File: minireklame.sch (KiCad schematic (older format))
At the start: 33 parts, among them IC1 ATXMEGA64A4U-A, P1 CONN_01X02, P10 CONN_01X04, P11 CONN_01X04, P12 CONN_01X04, P13 CONN_01X04, P14 CONN_01X04, P15 CONN_01X04, P16 CONN_01X04, P17 CONN_01X04, P2 CONN_01X04, P3 CONN_01X02, P3 CONN_01X04, P4 CONN_01X04, P5 CONN_01X04, P6 CONN_01X04, P7 CONN_01X04, P8 CONN_01X04, P9 CONN_01X04, U1 TLV1117-33CDCYR, U2 SP3483-EN-L, U3 TLC5955

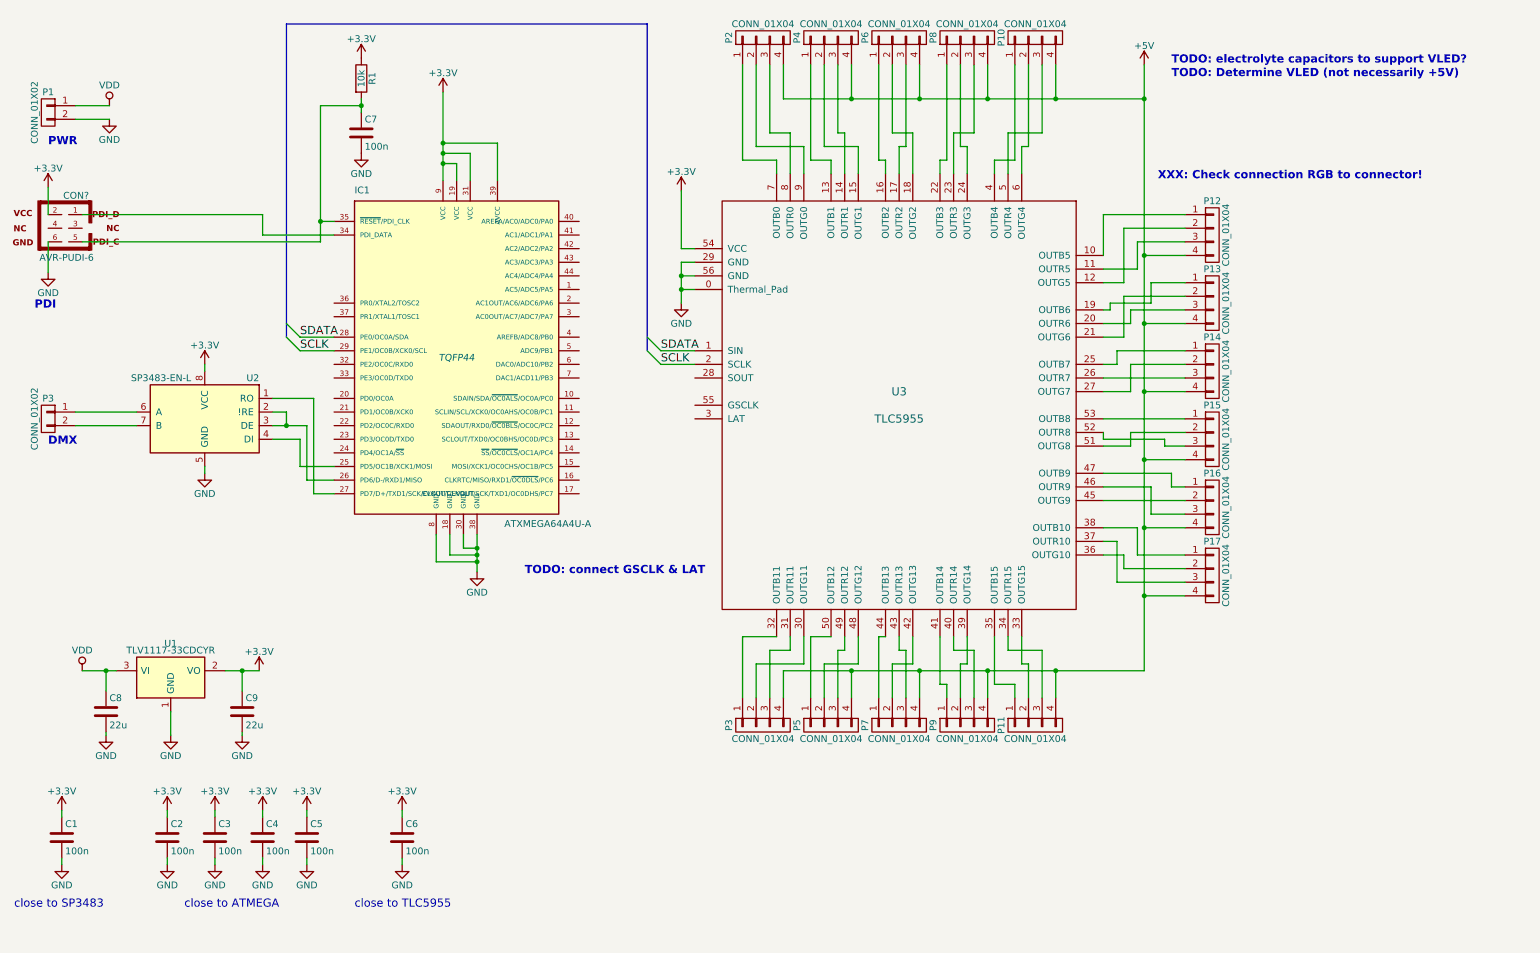
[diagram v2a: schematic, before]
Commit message: pulldown for & !RE DE line
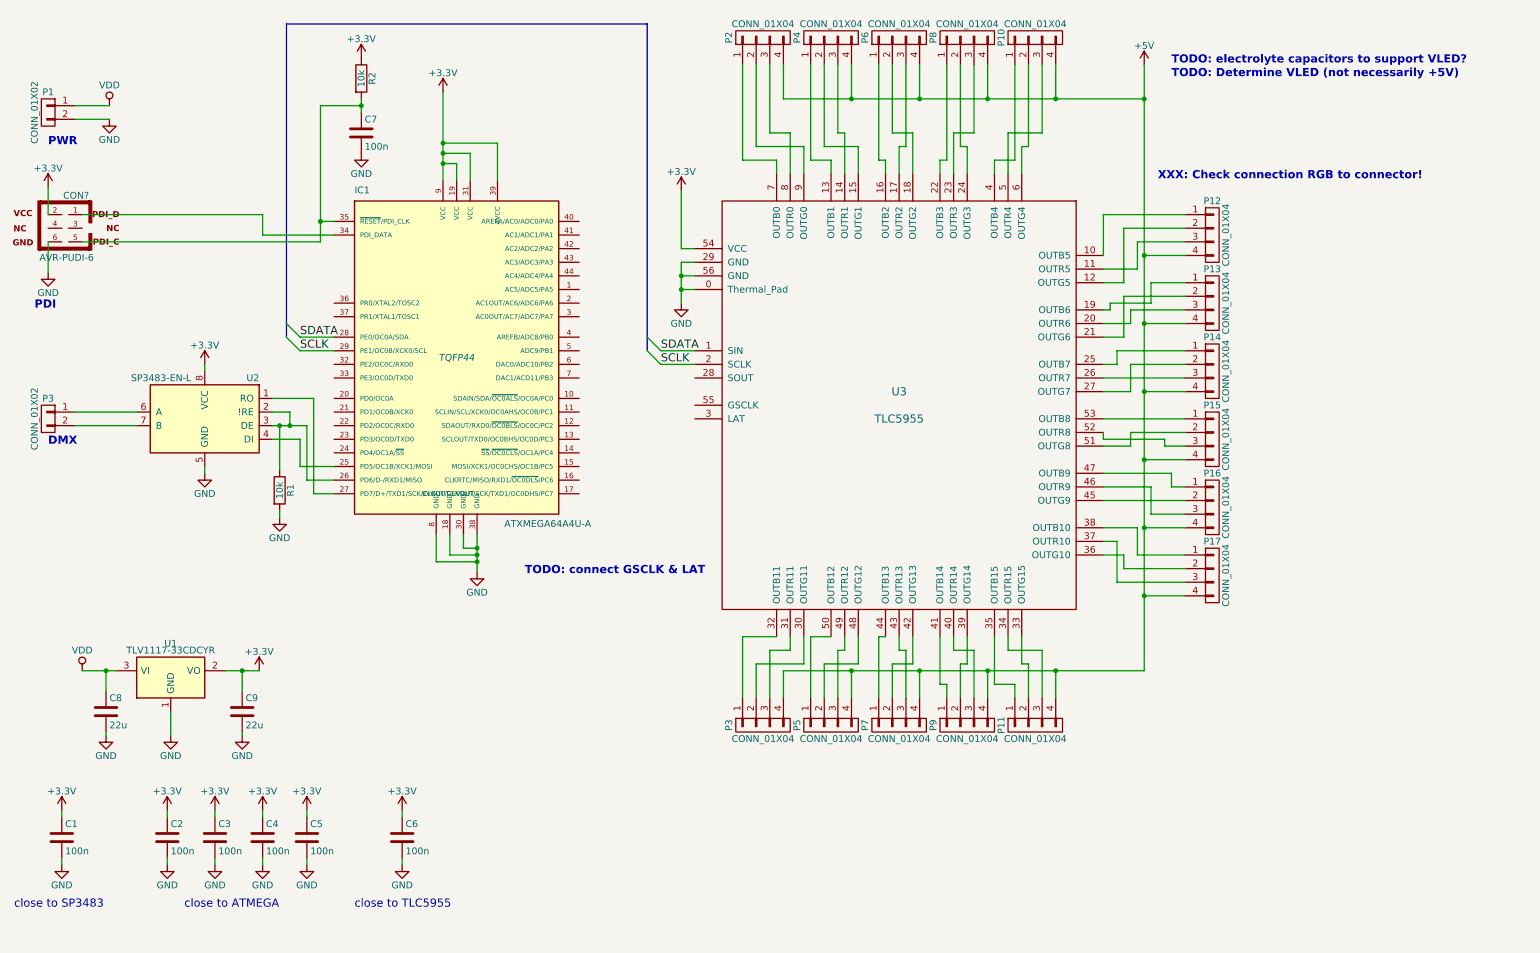
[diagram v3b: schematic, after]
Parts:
- added R1: 10k, symbol R
- renumbered R1 to R2
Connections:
- net GND: now also R1.2
- net at IC1.26 (PD6/D-/RXD1/MISO), U2.2 (!RE), U2.3 (DE): now also R1.1
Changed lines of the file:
@@
 	3700 4600 3700 4800
 Wire Wire Line
-	4000 4600 4000 4875
+	4000 4600 4000 4700
+Wire Wire Line
+	4000 4700 4000 4750
+Wire Wire Line
+	4000 4750 4000 4800
+Wire Wire Line
+	4000 4800 4000 4875
 Wire Wire Line
 	3900 4600 3900 4700
@@
 	5500 2800 5600 2800
 Wire Wire Line
-	5500 2600 5500 2900
+	5500 2600 5500 2700
+Wire Wire Line
+	5500 2700 5500 2800
+Wire Wire Line
+	5500 2800 5500 2900
 Wire Wire Line
 	5600 2700 5500 2700
@@
 Connection ~ 5500 2700
 Wire Wire Line
-	3750 1350 3750 2000
+	3750 1350 3750 1725
+Wire Wire Line
+	3750 1725 3750 1800
+Wire Wire Line
+	3750 1800 3750 1875
+Wire Wire Line
+	3750 1875 3750 2000
 Wire Wire Line
 	5500 2500 5600 2500
@@
 	5600 3350 5350 3350
 Wire Bus Line
-	5250 850  5250 3250
+	5250 850  5250 3150
+Wire Bus Line
+	5250 3150 5250 3250
 Wire Bus Line
 	5250 850  2600 850
 Wire Bus Line
-	2600 850  2600 3150
+	2600 850  2600 3050
+Wire Bus Line
+	2600 3050 2600 3150
 Wire Wire Line
 	2700 3150 2950 3150
@@
 	2700 4100 2950 4100
 Wire Wire Line
-	2500 3800 2750 3800
+	2500 3800 2550 3800
+Wire Wire Line
+	2550 3800 2625 3800
+Wire Wire Line
+	2625 3800 2750 3800
 Wire Wire Line
 	2750 3800 2750 4200
@@
 	2750 4200 2950 4200
 Wire Wire Line
-	2500 3700 2600 3700
-Wire Wire Line
-	2600 3700 2600 3800
-Connection ~ 2600 3800
+	2500 3700 2625 3700
+Wire Wire Line
+	2625 3700 2625 3800
+Connection ~ 2625 3800
 Wire Wire Line
 	2500 3600 2800 3600
@@
 	6250 1150 6250 1400
 Wire Wire Line
-	6250 1400 8900 1400
-Wire Wire Line
-	8900 5600 8900 1150
+	6250 1400 6750 1400
+Wire Wire Line
+	6750 1400 7250 1400
+Wire Wire Line
+	7250 1400 7750 1400
+Wire Wire Line
+	7750 1400 8250 1400
+Wire Wire Line
+	8250 1400 8900 1400
+Wire Wire Line
+	8900 5600 8900 5050
+Wire Wire Line
+	8900 5050 8900 4550
+Wire Wire Line
+	8900 4550 8900 4050
+Wire Wire Line
+	8900 4050 8900 3550
+Wire Wire Line
+	8900 3550 8900 3050
+Wire Wire Line
+	8900 3050 8900 2550
+Wire Wire Line
+	8900 2550 8900 1400
+Wire Wire Line
+	8900 1400 8900 1150
 Wire Wire Line
 	6750 1150 6750 1400
@@
 	6250 5800 6250 5600
 Wire Wire Line
-	6250 5600 8900 5600
+	6250 5600 6750 5600
+Wire Wire Line
+	6750 5600 7250 5600
+Wire Wire Line
+	7250 5600 7750 5600
+Wire Wire Line
+	7750 5600 8250 5600
+Wire Wire Line
+	8250 5600 8900 5600
 Connection ~ 8900 5050
 Wire Wire Line
@@
 $EndComp
 Wire Wire Line
-	1100 5600 1350 5600
+	1100 5600 1275 5600
+Wire Wire Line
+	1275 5600 1350 5600
 $Comp
 L GND #PWR012
@@
 TODO: Determine VLED (not necessarily +5V)
 $Comp
-L R R1
+L R R2
 U 1 1 58DDA6F7
 P 3150 1250
-F 0 "R1" V 3230 1250 50  0000 C CNN
+F 0 "R2" V 3230 1250 50  0000 C CNN
 F 1 "10k" V 3150 1250 50  0000 C CNN
 F 2 "" V 3080 1250 50  0001 C CNN
@@
 	2850 1450 3150 1450
 Wire Wire Line
-	3150 1400 3150 1500
+	3150 1400 3150 1450
+Wire Wire Line
+	3150 1450 3150 1500
 Connection ~ 3150 1450
 $Comp
@@
 	1050 1550 1300 1550
 Wire Wire Line
-	2850 1450 2850 2450
+	2850 1450 2850 2300
+Wire Wire Line
+	2850 2300 2850 2450
 Text Notes 850  1750 0    60   ~ 12
 PWR
@@
 	1750 5900 1750 6075
 Wire Wire Line
-	2150 5600 2400 5600
+	2150 5600 2275 5600
+Wire Wire Line
+	2275 5600 2400 5600
 Wire Wire Line
 	2275 5750 2275 5600
@@
 Wire Wire Line
 	5600 2600 5500 2600
+$Comp
+L R R1
+U 1 1 591A7EA8
+P 2550 4275
+F 0 "R1" V 2630 4275 50  0000 C CNN
+F 1 "10k" V 2550 4275 50  0000 C CNN
+F 2 "" V 2480 4275 50  0001 C CNN
+F 3 "" H 2550 4275 50  0001 C CNN
+	1    2550 4275
+	1    0    0    -1
+$EndComp
+$Comp
+L GND #PWR?
+U 1 1 591A821A
+P 2550 4475
+F 0 "#PWR?" H 2550 4225 50  0001 C CNN
+F 1 "GND" H 2550 4325 50  0000 C CNN
+F 2 "" H 2550 4475 50  0000 C CNN
+F 3 "" H 2550 4475 50  0000 C CNN
+	1    2550 4475
+	1    0    0    -1
+$EndComp
+Wire Wire Line
+	2550 4475 2550 4425
+Wire Wire Line
+	2550 4125 2550 3800
+Connection ~ 2550 3800
 $EndSCHEMATC

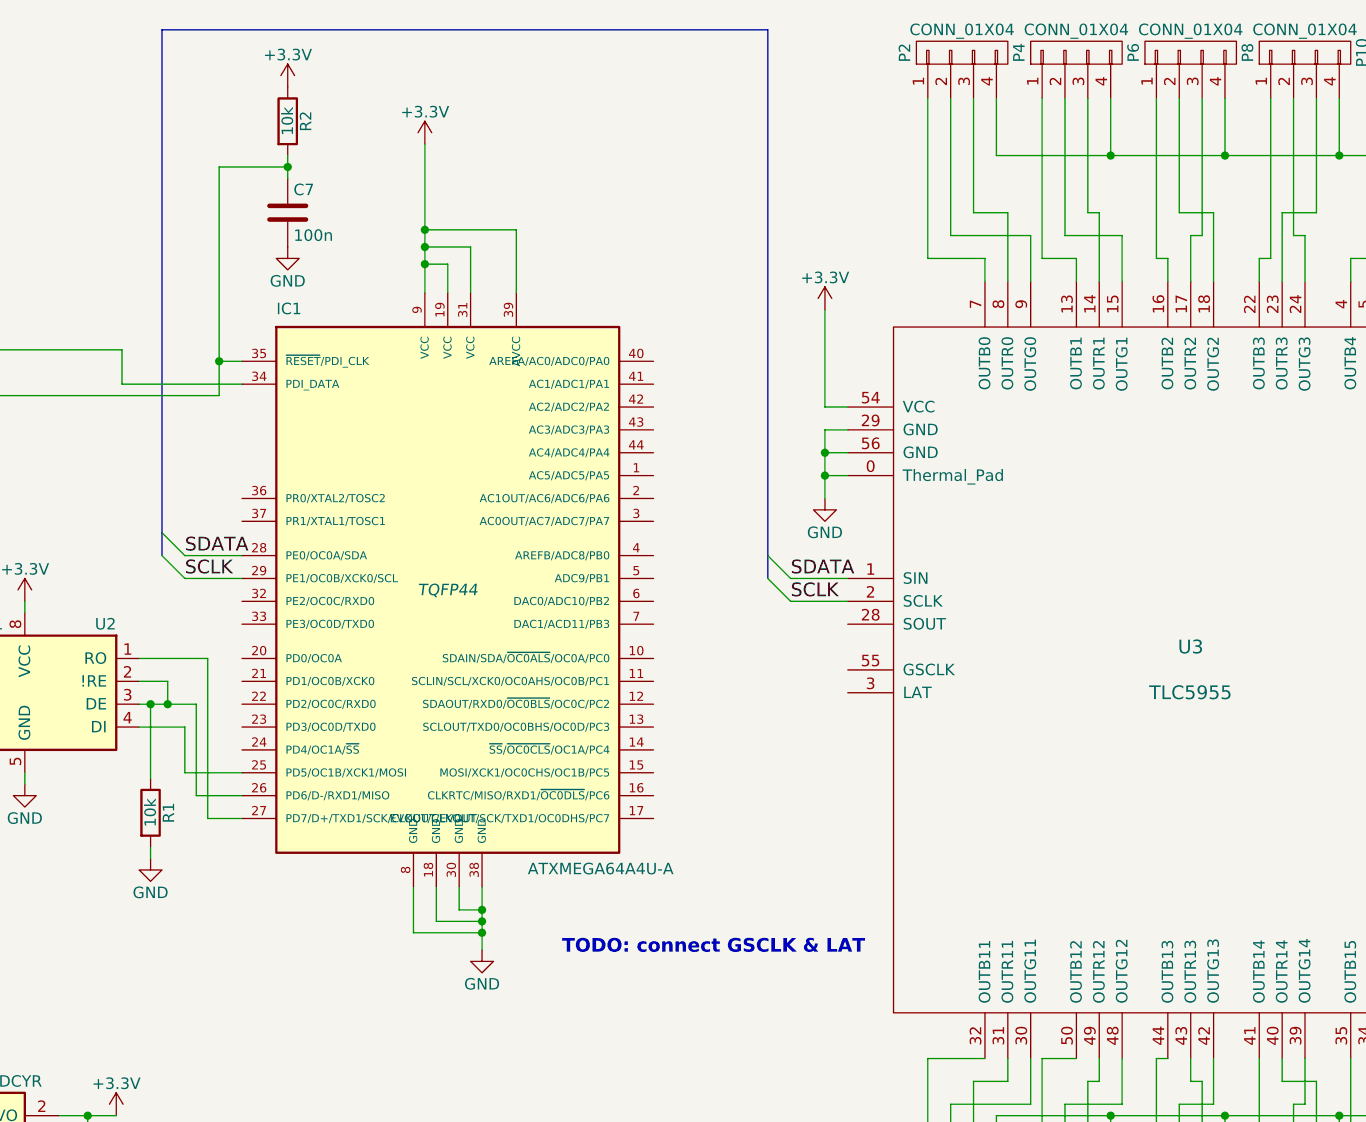
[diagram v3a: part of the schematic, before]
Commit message: fixing ATXMEGA TLC conncetion
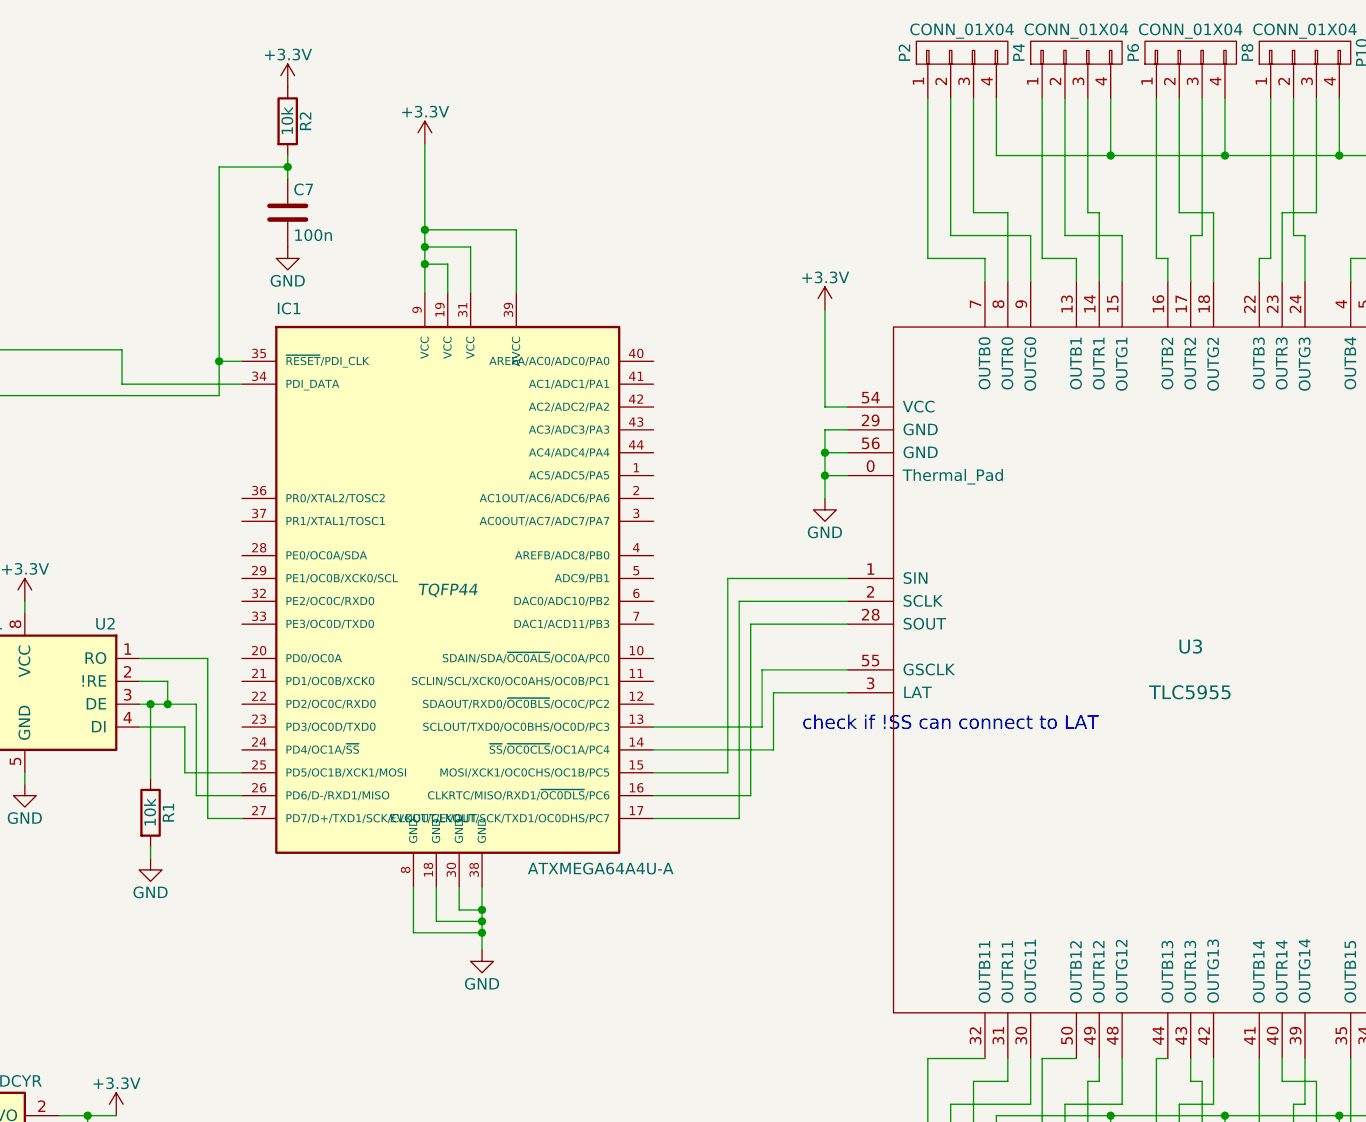
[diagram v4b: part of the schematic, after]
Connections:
- net at U3.28 (SOUT): now also IC1.16 (CLKRTC/MISO/RXD1/~OC0DLS~/PC6)
- net at U3.3 (LAT): now also IC1.14 (~SS~/~OC0CLS~/OC1A/PC4)
- net at U3.55 (GSCLK): now also IC1.13 (SCLOUT/TXD0/OC0BHS/OC0D/PC3)
- net at IC1.15 (MOSI/XCK1/OC0CHS/OC1B/PC5): now also U3.1 (SIN)
- net at IC1.17 (EVOUT/CLKOUT/SCK/TXD1/OC0DHS/PC7): now also U3.2 (SCLK)
- net SCLK: no longer names the net of IC1.29 (PE1/OC0B/XCK0/SCL)
- net SCLK: no longer U3.2 (SCLK)
- net SDATA: no longer names the net of IC1.28 (PE0/OC0A/SDA)
- net SDATA: no longer U3.1 (SIN)
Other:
- note added: "check if !SS can connect to LAT"
- note removed: "TODO: connect GSCLK & LAT"
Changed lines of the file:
@@
 	1    0    0    -1
 $EndComp
-Text Label 5350 3250 0    60   ~ 0
-SDATA
-Text Label 5350 3350 0    60   ~ 0
-SCLK
-Entry Wire Line
-	5250 3150 5350 3250
-Entry Wire Line
-	5250 3250 5350 3350
-Entry Wire Line
-	2600 3050 2700 3150
-Entry Wire Line
-	2600 3150 2700 3250
-Text Label 2700 3150 0    60   ~ 0
-SDATA
-Text Label 2700 3250 0    60   ~ 0
-SCLK
 $Comp
 L C C2
@@
 	5500 2075 5500 2500
 Wire Wire Line
-	5600 3250 5350 3250
-Wire Wire Line
-	5600 3350 5350 3350
-Wire Bus Line
-	5250 850  5250 3150
-Wire Bus Line
-	5250 3150 5250 3250
-Wire Bus Line
-	5250 850  2600 850
-Wire Bus Line
-	2600 850  2600 3050
-Wire Bus Line
-	2600 3050 2600 3150
-Wire Wire Line
-	2700 3150 2950 3150
-Wire Wire Line
-	2950 3250 2700 3250
-Wire Wire Line
 	2500 3900 2700 3900
 Wire Wire Line
@@
 Text Notes 850  3950 0    60   ~ 12
 DMX
-Text Notes 4350 4900 0    60   ~ 12
-TODO: connect GSCLK & LAT
 $Comp
 L AVR-PUDI-6 CON?
@@
 	2550 4125 2550 3800
 Connection ~ 2550 3800
+Wire Wire Line
+	4750 4200 5175 4200
+Wire Wire Line
+	5175 4200 5175 3450
+Wire Wire Line
+	5175 3450 5600 3450
+Wire Wire Line
+	4750 4100 5075 4100
+Wire Wire Line
+	5075 4100 5075 3250
+Wire Wire Line
+	5075 3250 5600 3250
+Wire Wire Line
+	4750 4300 5125 4300
+Wire Wire Line
+	5125 4300 5125 3350
+Wire Wire Line
+	5125 3350 5600 3350
+Wire Wire Line
+	4750 4000 5275 4000
+Wire Wire Line
+	5275 4000 5275 3750
+Wire Wire Line
+	5275 3750 5600 3750
+Wire Wire Line
+	4750 3900 5225 3900
+Wire Wire Line
+	5225 3900 5225 3650
+Wire Wire Line
+	5225 3650 5600 3650
+Text Notes 5400 3925 0    60   ~ 0
+check if !SS can connect to LAT
 $EndSCHEMATC
